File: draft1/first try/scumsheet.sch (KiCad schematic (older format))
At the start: 2 parts, among them U8? scum3

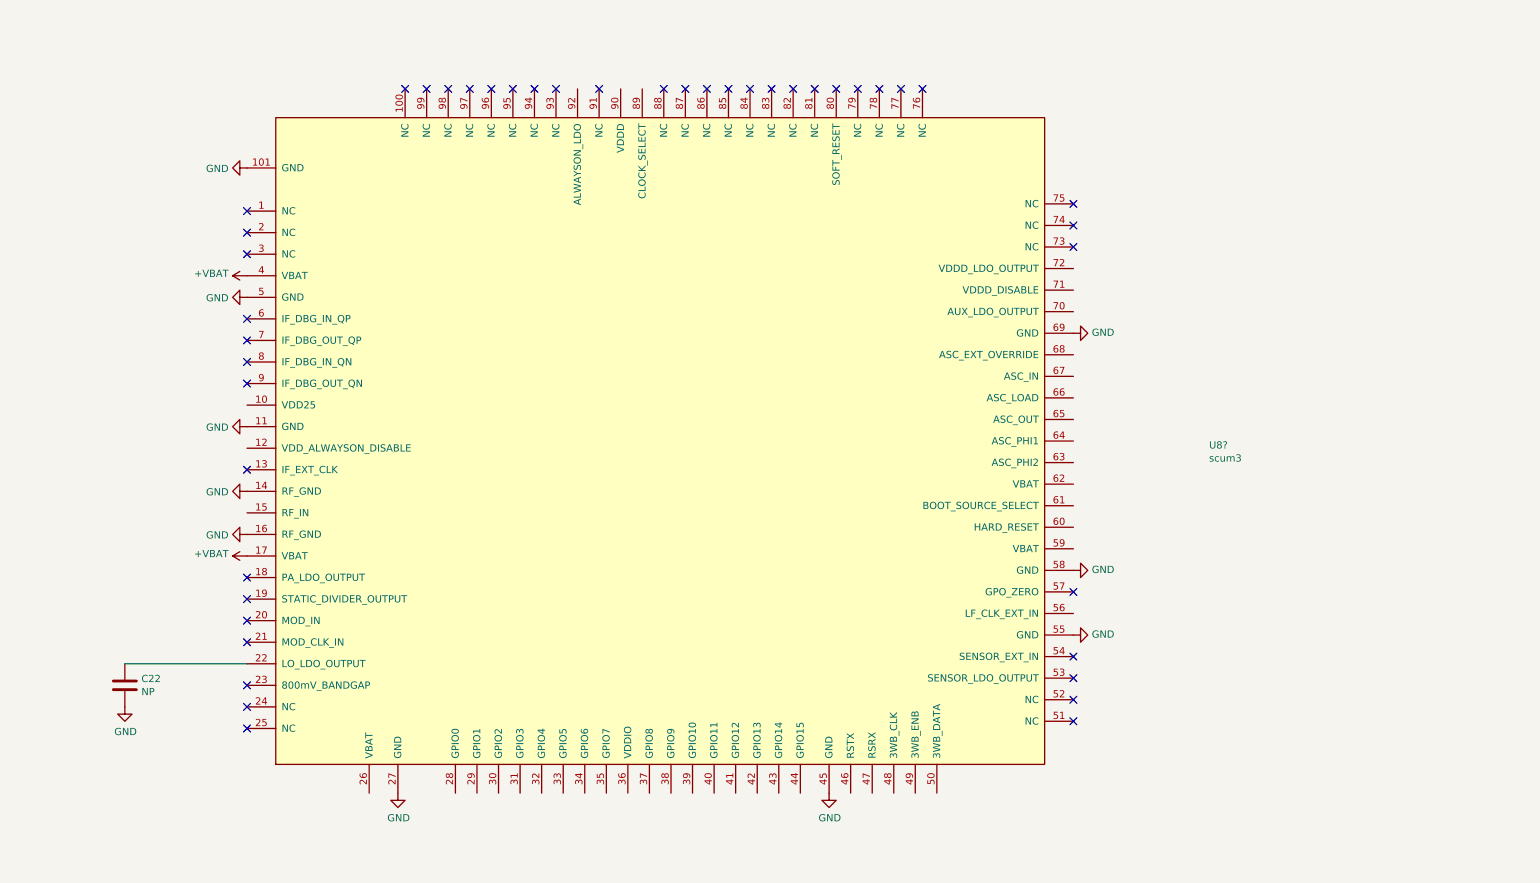
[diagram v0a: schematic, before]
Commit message: added gpio labels
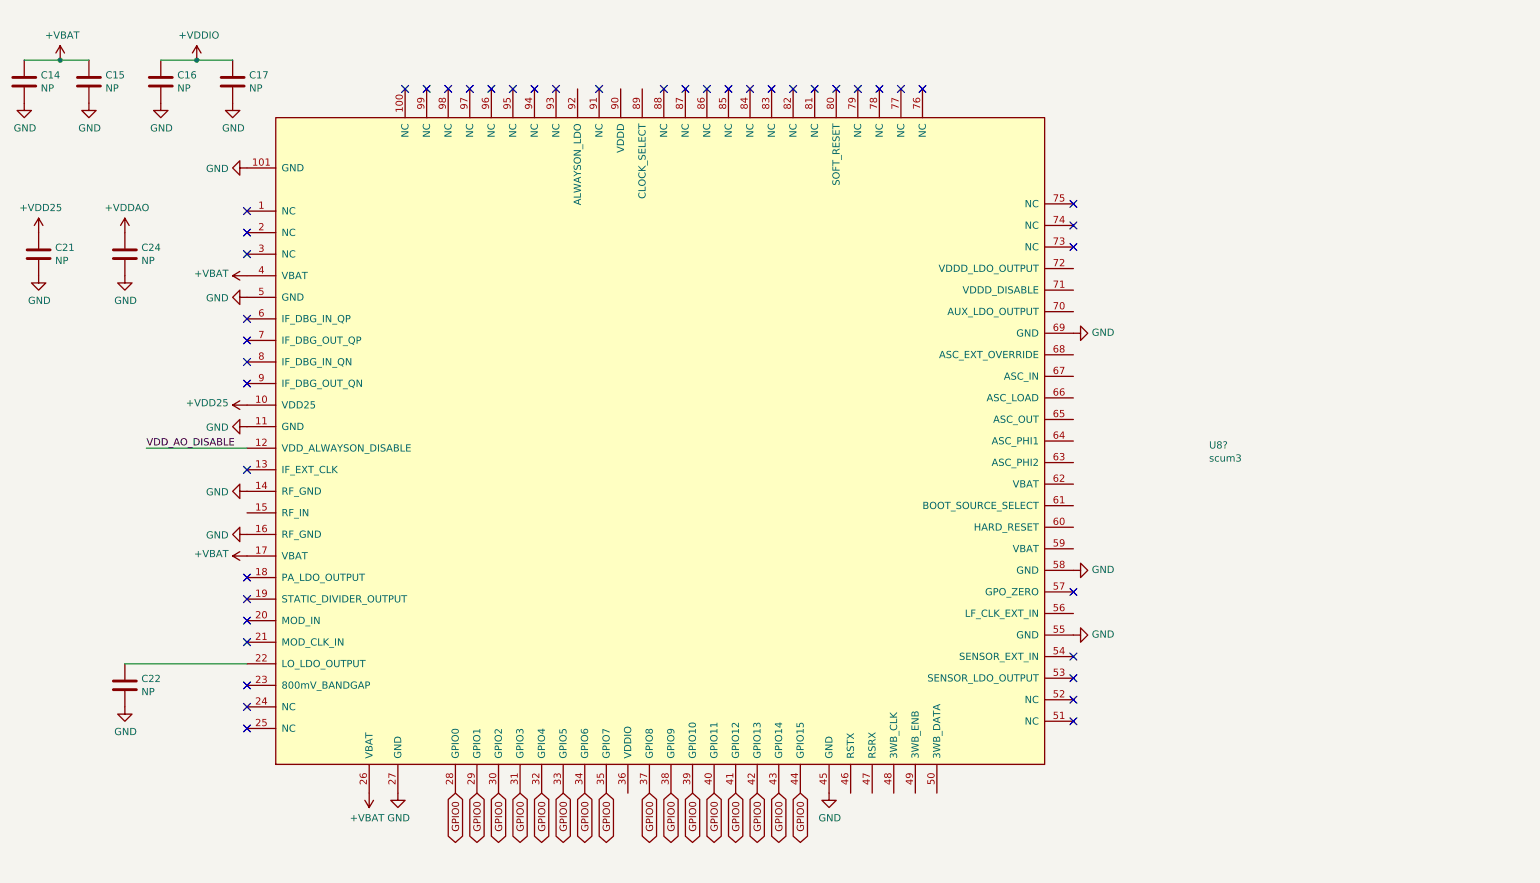
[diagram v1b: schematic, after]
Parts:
- added C14, C15, C16, C17, C21, C24: NP, symbol Device:C
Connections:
- net +VBAT: now also U8?.26 (VBAT), C14.1, C15.1
- net GND: now also C14.2, C15.2, C16.2, C17.2, C21.2, C24.2
- net +VDD25: now reaches U8?.10 (VDD25)
- net +VDD25: now also C21.1
- net VDD_AO_DISABLE: now reaches U8?.12 (VDD_ALWAYSON_DISABLE)
- net GPIO0: now reaches U8?.28 (GPIO0)
- net GPIO0: now also U8?.29 (GPIO1), U8?.30 (GPIO2), U8?.31 (GPIO3), U8?.32 (GPIO4), U8?.33 (GPIO5), U8?.34 (GPIO6), U8?.35 (GPIO7), U8?.37 (GPIO8), U8?.38 (GPIO9), U8?.39 (GPIO10), U8?.40 (GPIO11), U8?.41 (GPIO12), U8?.42 (GPIO13), U8?.43 (GPIO14), U8?.44 (GPIO15)
- new net +VDDAO: C24.1
- new net +VDDIO: C16.1, C17.1

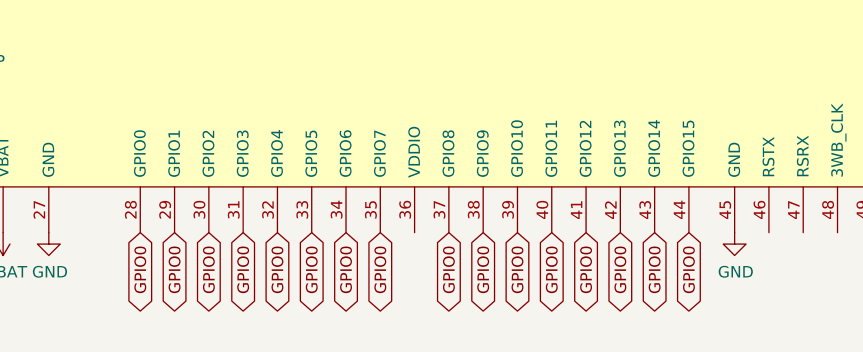
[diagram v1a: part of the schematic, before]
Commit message: labeled gpios
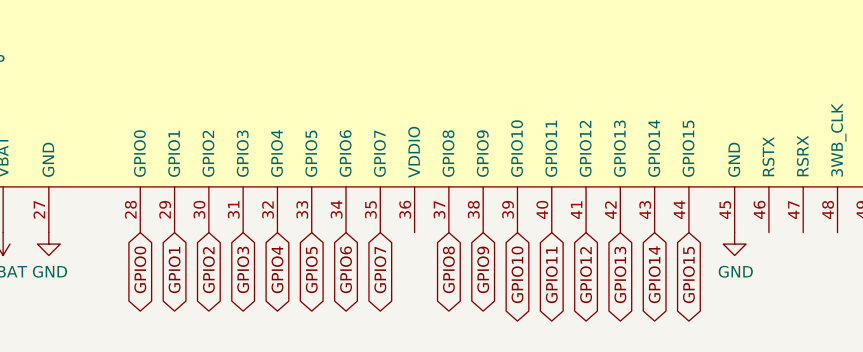
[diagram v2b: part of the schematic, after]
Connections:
- net GPIO0: no longer U8?.29 (GPIO1), U8?.30 (GPIO2), U8?.31 (GPIO3), U8?.32 (GPIO4), U8?.33 (GPIO5), U8?.34 (GPIO6), U8?.35 (GPIO7), U8?.37 (GPIO8), U8?.38 (GPIO9), U8?.39 (GPIO10), U8?.40 (GPIO11), U8?.41 (GPIO12), U8?.42 (GPIO13), U8?.43 (GPIO14), U8?.44 (GPIO15)
- new net GPIO1: U8?.29 (GPIO1)
- new net GPIO10: U8?.39 (GPIO10)
- new net GPIO11: U8?.40 (GPIO11)
- new net GPIO12: U8?.41 (GPIO12)
- new net GPIO13: U8?.42 (GPIO13)
- new net GPIO14: U8?.43 (GPIO14)
- new net GPIO15: U8?.44 (GPIO15)
- new net GPIO2: U8?.30 (GPIO2)
- new net GPIO3: U8?.31 (GPIO3)
- new net GPIO4: U8?.32 (GPIO4)
- new net GPIO5: U8?.33 (GPIO5)
- new net GPIO6: U8?.34 (GPIO6)
- new net GPIO7: U8?.35 (GPIO7)
- new net GPIO8: U8?.37 (GPIO8)
- new net GPIO9: U8?.38 (GPIO9)
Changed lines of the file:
@@
 GPIO0
 Text GLabel 3850 6050 3    50   BiDi ~ 0
-GPIO0
+GPIO1
 Text GLabel 4000 6050 3    50   BiDi ~ 0
-GPIO0
+GPIO2
 Text GLabel 4150 6050 3    50   BiDi ~ 0
-GPIO0
+GPIO3
 Text GLabel 4300 6050 3    50   BiDi ~ 0
-GPIO0
+GPIO4
 Text GLabel 4450 6050 3    50   BiDi ~ 0
-GPIO0
+GPIO5
 Text GLabel 4600 6050 3    50   BiDi ~ 0
-GPIO0
+GPIO6
 Text GLabel 4750 6050 3    50   BiDi ~ 0
-GPIO0
+GPIO7
 Text GLabel 5050 6050 3    50   BiDi ~ 0
-GPIO0
+GPIO8
 Text GLabel 5200 6050 3    50   BiDi ~ 0
-GPIO0
+GPIO9
 Text GLabel 5350 6050 3    50   BiDi ~ 0
-GPIO0
+GPIO10
 Text GLabel 5500 6050 3    50   BiDi ~ 0
-GPIO0
+GPIO11
 Text GLabel 5650 6050 3    50   BiDi ~ 0
-GPIO0
+GPIO12
 Text GLabel 5800 6050 3    50   BiDi ~ 0
-GPIO0
+GPIO13
 Text GLabel 5950 6050 3    50   BiDi ~ 0
-GPIO0
+GPIO14
 Text GLabel 6100 6050 3    50   BiDi ~ 0
-GPIO0
+GPIO15
 $EndSCHEMATC

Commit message: finished bottom pins
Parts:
- added C20: NP, symbol Device:C
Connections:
- net +VBAT: now also U8?.59 (VBAT), U8?.62 (VBAT)
- net +VDDIO: now also U8?.36 (VDDIO)
- net GND: now also C20.1
- net RsTx: now reaches U8?.46 (RSTX)
- net RsRx: now reaches U8?.47 (RSRX)
- net 3WB_CLK: now reaches U8?.48 (3WB_CLK)
- net 3WB_ENB: now reaches U8?.49 (3WB_ENB)
- net 3WB_DATA: now reaches U8?.50 (3WB_DATA)
- net LF_CLK_EXT_IN: now reaches U8?.56 (LF_CLK_EXT_IN)
- net HARD_RESETT: now reaches U8?.60 (HARD_RESET)
- net BOOT_SOURCE_SEL: now reaches U8?.61 (BOOT_SOURCE_SELECT)
- net ASC_PHI2: now reaches U8?.63 (ASC_PHI2)
- net ASC_PHI1: now reaches U8?.64 (ASC_PHI1)
- net ASC_OUT: now reaches U8?.65 (ASC_OUT)
- net ASC_LOAD: now reaches U8?.66 (ASC_LOAD)
- net ASC_IN: now reaches U8?.67 (ASC_IN)
- net ASC_EXT_override: now reaches U8?.68 (ASC_EXT_OVERRIDE)
- net at U8?.70 (AUX_LDO_OUTPUT): now also C20.2
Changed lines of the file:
@@
 Text GLabel 6100 6050 3    50   BiDi ~ 0
 GPIO15
+$Comp
+L draft1library:+VDDIO #PWR?
+U 1 1 5F404D67
+P 4900 6050
+F 0 "#PWR?" H 4900 5900 50  0001 C CNN
+F 1 "+VDDIO" H 4915 6223 50  0000 C CNN
+F 2 "" H 4900 6050 50  0001 C CNN
+F 3 "" H 4900 6050 50  0001 C CNN
+	1    4900 6050
+	-1   0    0    1
+$EndComp
+Text GLabel 6450 6050 3    50   Output ~ 0
+RsTx
+Text GLabel 6600 6050 3    50   Input ~ 0
+RsRx
+Text GLabel 6750 6050 3    50   Input ~ 0
+3WB_CLK
+Text GLabel 6900 6050 3    50   Input ~ 0
+3WB_ENB
+Text GLabel 7050 6050 3    50   Input ~ 0
+3WB_DATA
+Text GLabel 8000 4800 2    50   BiDi ~ 0
+LF_CLK_EXT_IN
+Text GLabel 8000 4200 2    50   BiDi ~ 0
+HARD_RESETT
+$Comp
+L draft1library:+VBAT #PWR?
+U 1 1 5F406DAE
+P 8000 4350
+F 0 "#PWR?" H 8000 4200 50  0001 C CNN
+F 1 "+VBAT" V 8015 4478 50  0000 L CNN
+F 2 "" H 8000 4350 50  0001 C CNN
+F 3 "" H 8000 4350 50  0001 C CNN
+	1    8000 4350
+	0    1    1    0
+$EndComp
+Text GLabel 8000 3750 2    50   BiDi ~ 0
+ASC_PHI2
+$Comp
+L draft1library:+VBAT #PWR?
+U 1 1 5F407E52
+P 8000 3900
+F 0 "#PWR?" H 8000 3750 50  0001 C CNN
+F 1 "+VBAT" V 8015 4028 50  0000 L CNN
+F 2 "" H 8000 3900 50  0001 C CNN
+F 3 "" H 8000 3900 50  0001 C CNN
+	1    8000 3900
+	0    1    1    0
+$EndComp
+Wire Wire Line
+	8000 4050 9250 4050
+Text Label 9250 4050 0    50   ~ 0
+BOOT_SOURCE_SEL
+Text GLabel 8000 3600 2    50   BiDi ~ 0
+ASC_PHI1
+Text GLabel 8000 3450 2    50   BiDi ~ 0
+ASC_OUT
+Text GLabel 8000 3300 2    50   BiDi ~ 0
+ASC_LOAD
+Text GLabel 8000 3150 2    50   BiDi ~ 0
+ASC_IN
+Text GLabel 8000 3000 2    50   BiDi ~ 0
+ASC_EXT_override
+$Comp
+L Device:C C20
+U 1 1 5F40AC2A
+P 8850 2700
+F 0 "C20" H 8965 2746 50  0000 L CNN
+F 1 "NP" H 8965 2655 50  0000 L CNN
+F 2 "" H 8888 2550 50  0001 C CNN
+F 3 "~" H 8850 2700 50  0001 C CNN
+	1    8850 2700
+	0    1    1    0
+$EndComp
+Wire Wire Line
+	8000 2700 8700 2700
+$Comp
+L power:GND #PWR?
+U 1 1 5F40CD8D
+P 9000 2700
+F 0 "#PWR?" H 9000 2450 50  0001 C CNN
+F 1 "GND" V 9005 2572 50  0000 R CNN
+F 2 "" H 9000 2700 50  0001 C CNN
+F 3 "" H 9000 2700 50  0001 C CNN
+	1    9000 2700
+	0    -1   -1   0
+$EndComp
 $EndSCHEMATC

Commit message: finished right side
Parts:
- added C18 (x2): NP, symbol Device:C
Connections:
- net GND: now also C18.1, C18.1
- net AUX_LDO_OUTPUT: now reaches C20.2, U8?.70 (AUX_LDO_OUTPUT)
- net VDDD_DISABLE: now reaches U8?.71 (VDDD_DISABLE)
- net +VDDD: now reaches U8?.72 (VDDD_LDO_OUTPUT)
- net +VDDD: now also C18.2, C18.2
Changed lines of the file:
@@
 	0    -1   -1   0
 $EndComp
+Text Label 8050 2700 0    50   ~ 0
+AUX_LDO_OUTPUT
+Wire Wire Line
+	8000 2550 8700 2550
+Text Label 8700 2550 0    50   ~ 0
+VDDD_DISABLE
+$Comp
+L Device:C C18
+U 1 1 5F40EBE3
+P 8950 1800
+F 0 "C18" H 9065 1846 50  0000 L CNN
+F 1 "NP" H 9065 1755 50  0000 L CNN
+F 2 "" H 8988 1650 50  0001 C CNN
+F 3 "~" H 8950 1800 50  0001 C CNN
+	1    8950 1800
+	0    1    1    0
+$EndComp
+$Comp
+L Device:C C18
+U 1 1 5F40F3CB
+P 8950 2150
+F 0 "C18" H 9065 2196 50  0000 L CNN
+F 1 "NP" H 9065 2105 50  0000 L CNN
+F 2 "" H 8988 2000 50  0001 C CNN
+F 3 "~" H 8950 2150 50  0001 C CNN
+	1    8950 2150
+	0    1    1    0
+$EndComp
+$Comp
+L power:GND #PWR?
+U 1 1 5F40F9FD
+P 9100 2150
+F 0 "#PWR?" H 9100 1900 50  0001 C CNN
+F 1 "GND" V 9105 2022 50  0000 R CNN
+F 2 "" H 9100 2150 50  0001 C CNN
+F 3 "" H 9100 2150 50  0001 C CNN
+	1    9100 2150
+	0    -1   -1   0
+$EndComp
+Wire Wire Line
+	9100 1800 9100 2150
+Connection ~ 9100 2150
+$Comp
+L draft1library:+VDDD #PWR?
+U 1 1 5F410A04
+P 8800 1800
+F 0 "#PWR?" H 8800 1650 50  0001 C CNN
+F 1 "+VDDD" H 8815 1973 50  0000 C CNN
+F 2 "" H 8800 1800 50  0001 C CNN
+F 3 "" H 8800 1800 50  0001 C CNN
+	1    8800 1800
+	1    0    0    -1
+$EndComp
+Wire Wire Line
+	8800 1800 8800 2150
+Connection ~ 8800 1800
+Wire Wire Line
+	8800 2150 8800 2400
+Wire Wire Line
+	8800 2400 8000 2400
+Connection ~ 8800 2150
 $EndSCHEMATC

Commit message: labeled something idk
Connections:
- wire segments 13 -> 14
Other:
- note added: "idk what goes here"
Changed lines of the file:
@@
 	8800 2400 8000 2400
 Connection ~ 8800 2150
+$Comp
+L power:GND #PWR?
+U 1 1 5F4157E6
+P 800 4400
+F 0 "#PWR?" H 800 4150 50  0001 C CNN
+F 1 "GND" H 805 4227 50  0000 C CNN
+F 2 "" H 800 4400 50  0001 C CNN
+F 3 "" H 800 4400 50  0001 C CNN
+	1    800  4400
+	1    0    0    -1
+$EndComp
+Wire Wire Line
+	2250 4100 900  4100
+Text Notes 700  4250 0    50   ~ 0
+idk what goes here
 $EndSCHEMATC

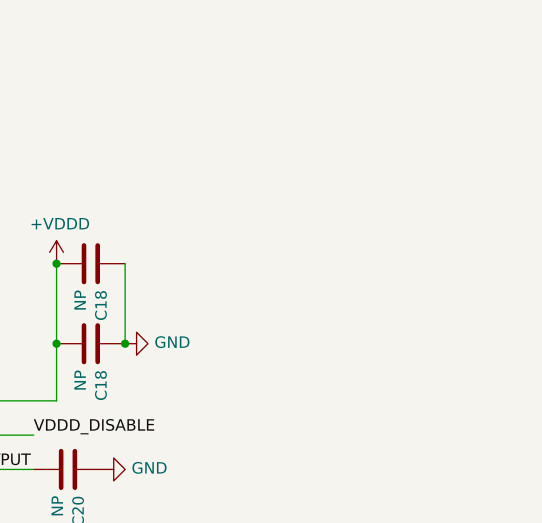
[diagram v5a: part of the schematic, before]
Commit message: added resistors
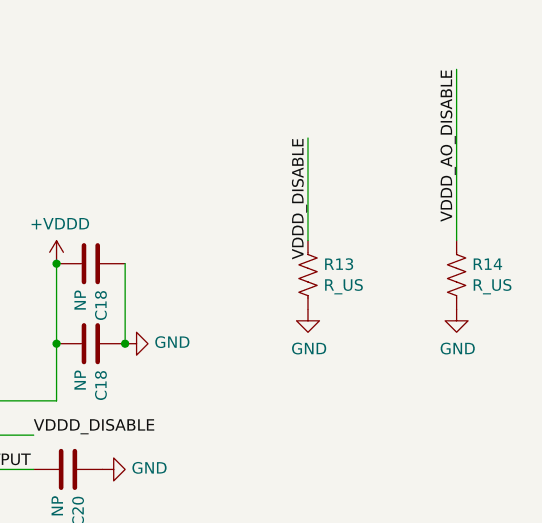
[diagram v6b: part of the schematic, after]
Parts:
- added R13, R14: R_US, symbol Device:R_US
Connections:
- net labels added: VDDD_AO_DISABLE
- wire segments 14 -> 16
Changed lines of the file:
@@
 Text Notes 700  4250 0    50   ~ 0
 idk what goes here
+$Comp
+L Device:R_US R13
+U 1 1 5F4188E4
+P 9900 1850
+F 0 "R13" H 9968 1896 50  0000 L CNN
+F 1 "R_US" H 9968 1805 50  0000 L CNN
+F 2 "" V 9940 1840 50  0001 C CNN
+F 3 "~" H 9900 1850 50  0001 C CNN
+	1    9900 1850
+	1    0    0    -1
+$EndComp
+$Comp
+L Device:R_US R14
+U 1 1 5F419870
+P 10550 1850
+F 0 "R14" H 10618 1896 50  0000 L CNN
+F 1 "R_US" H 10618 1805 50  0000 L CNN
+F 2 "" V 10590 1840 50  0001 C CNN
+F 3 "~" H 10550 1850 50  0001 C CNN
+	1    10550 1850
+	1    0    0    -1
+$EndComp
+$Comp
+L power:GND #PWR?
+U 1 1 5F419E58
+P 9900 2000
+F 0 "#PWR?" H 9900 1750 50  0001 C CNN
+F 1 "GND" H 9905 1827 50  0000 C CNN
+F 2 "" H 9900 2000 50  0001 C CNN
+F 3 "" H 9900 2000 50  0001 C CNN
+	1    9900 2000
+	1    0    0    -1
+$EndComp
+$Comp
+L power:GND #PWR?
+U 1 1 5F41A5FE
+P 10550 2000
+F 0 "#PWR?" H 10550 1750 50  0001 C CNN
+F 1 "GND" H 10555 1827 50  0000 C CNN
+F 2 "" H 10550 2000 50  0001 C CNN
+F 3 "" H 10550 2000 50  0001 C CNN
+	1    10550 2000
+	1    0    0    -1
+$EndComp
+Wire Wire Line
+	9900 1700 9900 1250
+Text Label 9900 1250 3    50   ~ 0
+VDDD_DISABLE
+Wire Wire Line
+	10550 1700 10550 950
+Text Label 10550 950  3    50   ~ 0
+VDDD_AO_DISABLE
 $EndSCHEMATC

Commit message: added temp sensor
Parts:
- added C23: NP, symbol Device:C
- added IC?: ADT7302ARMZ, SOP65P490X110-8N, symbol SamacSys_Parts:ADT7302ARMZ
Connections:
- net labels added: GP4, GP5, GP6, GP7
- wire segments 16 -> 23
- no-connect marks 45 -> 46
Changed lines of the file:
@@
 Text Label 10550 950  3    50   ~ 0
 VDDD_AO_DISABLE
+$Comp
+L SamacSys_Parts:ADT7302ARMZ IC?
+U 1 1 5F38CA2F
+P 9350 5550
+F 0 "IC?" H 9900 5815 50  0000 C CNN
+F 1 "ADT7302ARMZ" H 9900 5724 50  0000 C CNN
+F 2 "SOP65P490X110-8N" H 10300 5650 50  0001 L CNN
+F 3 "" H 10300 5550 50  0001 L CNN
+F 4 "Digital Temperature Sensor" H 10300 5450 50  0001 L CNN "Description"
+F 5 "" H 10300 5350 50  0001 L CNN "Height"
+F 6 "Analog Devices" H 10300 5250 50  0001 L CNN "Manufacturer_Name"
+F 7 "ADT7302ARMZ" H 10300 5150 50  0001 L CNN "Manufacturer_Part_Number"
+F 8 "ADT7302ARMZ" H 10300 5050 50  0001 L CNN "Arrow Part Number"
+F 9 "https://www.arrow.com/en/products/adt7302armz/analog-devices" H 10300 4950 50  0001 L CNN "Arrow Price/Stock"
+F 10 "584-ADT7302ARMZ" H 10300 4850 50  0001 L CNN "Mouser Part Number"
+F 11 "https://www.mouser.co.uk/ProductDetail/Analog-Devices/ADT7302ARMZ?qs=WIvQP4zGanhRdU0rZVc2KQ%3D%3D" H 10300 4750 50  0001 L CNN "Mouser Price/Stock"
+	1    9350 5550
+	1    0    0    -1
+$EndComp
+Wire Wire Line
+	9350 5650 8800 5650
+Wire Wire Line
+	9350 5750 8800 5750
+Wire Wire Line
+	9350 5850 8800 5850
+$Comp
+L Device:C C23
+U 1 1 5F391C6F
+P 10450 6150
+F 0 "C23" H 10565 6196 50  0000 L CNN
+F 1 "NP" H 10565 6105 50  0000 L CNN
+F 2 "" H 10488 6000 50  0001 C CNN
+F 3 "~" H 10450 6150 50  0001 C CNN
+	1    10450 6150
+	1    0    0    -1
+$EndComp
+$Comp
+L power:GND #PWR?
+U 1 1 5F394492
+P 10450 6300
+F 0 "#PWR?" H 10450 6050 50  0001 C CNN
+F 1 "GND" H 10455 6127 50  0000 C CNN
+F 2 "" H 10450 6300 50  0001 C CNN
+F 3 "" H 10450 6300 50  0001 C CNN
+	1    10450 6300
+	1    0    0    -1
+$EndComp
+$Comp
+L draft1library:+VDDIO #PWR?
+U 1 1 5F394FE1
+P 10600 5850
+F 0 "#PWR?" H 10600 5700 50  0001 C CNN
+F 1 "+VDDIO" V 10615 5978 50  0000 L CNN
+F 2 "" H 10600 5850 50  0001 C CNN
+F 3 "" H 10600 5850 50  0001 C CNN
+	1    10600 5850
+	0    1    1    0
+$EndComp
+Wire Wire Line
+	10600 5850 10450 5850
+Wire Wire Line
+	10450 5850 10450 6000
+Connection ~ 10450 5850
+Wire Wire Line
+	10450 5750 10850 5750
+Wire Wire Line
+	10450 5650 10850 5650
+NoConn ~ 10450 5550
+Text Label 8800 5850 0    50   ~ 0
+GP4
+Text Label 10850 5750 0    50   ~ 0
+GP5
+Text Label 8800 5650 0    50   ~ 0
+GP6
+Text Label 8800 5750 0    50   ~ 0
+GP7
 $EndSCHEMATC

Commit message: finished scum sheet
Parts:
- added C13: NP, symbol Device:C
- added R12: R_US, symbol Device:R_US
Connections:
- wire segments 23 -> 32
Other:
- note added: "put a thing here"
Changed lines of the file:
@@
 Wire Wire Line
 	8000 4050 9250 4050
-Text Label 9250 4050 0    50   ~ 0
+Text Label 9250 4050 2    50   ~ 0
 BOOT_SOURCE_SEL
 Text GLabel 8000 3600 2    50   BiDi ~ 0
@@
 Wire Wire Line
 	8000 2550 8700 2550
-Text Label 8700 2550 0    50   ~ 0
+Text Label 8700 2550 2    50   ~ 0
 VDDD_DISABLE
 $Comp
@@
 Text Label 8800 5850 0    50   ~ 0
 GP4
-Text Label 10850 5750 0    50   ~ 0
+Text Label 10850 5750 2    50   ~ 0
 GP5
 Text Label 8800 5650 0    50   ~ 0
@@
 Text Label 8800 5750 0    50   ~ 0
 GP7
+$Comp
+L draft1library:+VDDAO #PWR?
+U 1 1 5F3A3049
+P 4550 1150
+F 0 "#PWR?" H 4550 1000 50  0001 C CNN
+F 1 "+VDDAO" H 4565 1323 50  0000 C CNN
+F 2 "" H 4550 1150 50  0001 C CNN
+F 3 "" H 4550 1150 50  0001 C CNN
+	1    4550 1150
+	1    0    0    -1
+$EndComp
+$Comp
+L power:GND #PWR?
+U 1 1 5F3A4A87
+P 3550 700
+F 0 "#PWR?" H 3550 450 50  0001 C CNN
+F 1 "GND" V 3555 572 50  0000 R CNN
+F 2 "" H 3550 700 50  0001 C CNN
+F 3 "" H 3550 700 50  0001 C CNN
+	1    3550 700
+	0    1    1    0
+$EndComp
+$Comp
+L Device:C C13
+U 1 1 5F3A5D08
+P 3700 700
+F 0 "C13" H 3815 746 50  0000 L CNN
+F 1 "NP" H 3815 655 50  0000 L CNN
+F 2 "" H 3738 550 50  0001 C CNN
+F 3 "~" H 3700 700 50  0001 C CNN
+	1    3700 700
+	0    1    1    0
+$EndComp
+$Comp
+L draft1library:+VDDD #PWR?
+U 1 1 5F3A7150
+P 4100 700
+F 0 "#PWR?" H 4100 550 50  0001 C CNN
+F 1 "+VDDD" H 4115 873 50  0000 C CNN
+F 2 "" H 4100 700 50  0001 C CNN
+F 3 "" H 4100 700 50  0001 C CNN
+	1    4100 700
+	-1   0    0    1
+$EndComp
+Wire Wire Line
+	4850 1150 4850 700
+Wire Wire Line
+	4850 700  4100 700
+Wire Wire Line
+	3850 700  4100 700
+Connection ~ 4100 700
+$Comp
+L draft1library:+VDDD #PWR?
+U 1 1 5F3A8DE4
+P 6000 700
+F 0 "#PWR?" H 6000 550 50  0001 C CNN
+F 1 "+VDDD" V 6015 828 50  0000 L CNN
+F 2 "" H 6000 700 50  0001 C CNN
+F 3 "" H 6000 700 50  0001 C CNN
+	1    6000 700
+	0    1    1    0
+$EndComp
+$Comp
+L Device:R_US R12
+U 1 1 5F3A9D0E
+P 5650 700
+F 0 "R12" H 5718 746 50  0000 L CNN
+F 1 "R_US" H 5718 655 50  0000 L CNN
+F 2 "" V 5690 690 50  0001 C CNN
+F 3 "~" H 5650 700 50  0001 C CNN
+	1    5650 700
+	0    1    1    0
+$EndComp
+Wire Wire Line
+	6000 700  5800 700
+Wire Wire Line
+	5500 700  5000 700
+Wire Wire Line
+	5000 700  5000 1150
+Text Notes 9650 4950 0    50   ~ 0
+put a thing here
+Wire Wire Line
+	10350 4900 10850 4900
+Wire Wire Line
+	10300 5050 10550 5050
+Wire Wire Line
+	10550 5050 10550 5150
+$Comp
+L draft1library:+VBAT #PWR?
+U 1 1 5F3AF896
+P 10550 5150
+F 0 "#PWR?" H 10550 5000 50  0001 C CNN
+F 1 "+VBAT" H 10565 5323 50  0000 C CNN
+F 2 "" H 10550 5150 50  0001 C CNN
+F 3 "" H 10550 5150 50  0001 C CNN
+	1    10550 5150
+	-1   0    0    1
+$EndComp
+Text Label 10350 4900 0    50   ~ 0
+BOOT_SOURCE_SEL
+$Comp
+L power:GND #PWR?
+U 1 1 5F3B118E
+P 10850 5650
+F 0 "#PWR?" H 10850 5400 50  0001 C CNN
+F 1 "GND" V 10855 5522 50  0000 R CNN
+F 2 "" H 10850 5650 50  0001 C CNN
+F 3 "" H 10850 5650 50  0001 C CNN
+	1    10850 5650
+	0    -1   -1   0
+$EndComp
 $EndSCHEMATC
